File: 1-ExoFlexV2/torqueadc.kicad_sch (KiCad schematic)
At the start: 54 parts

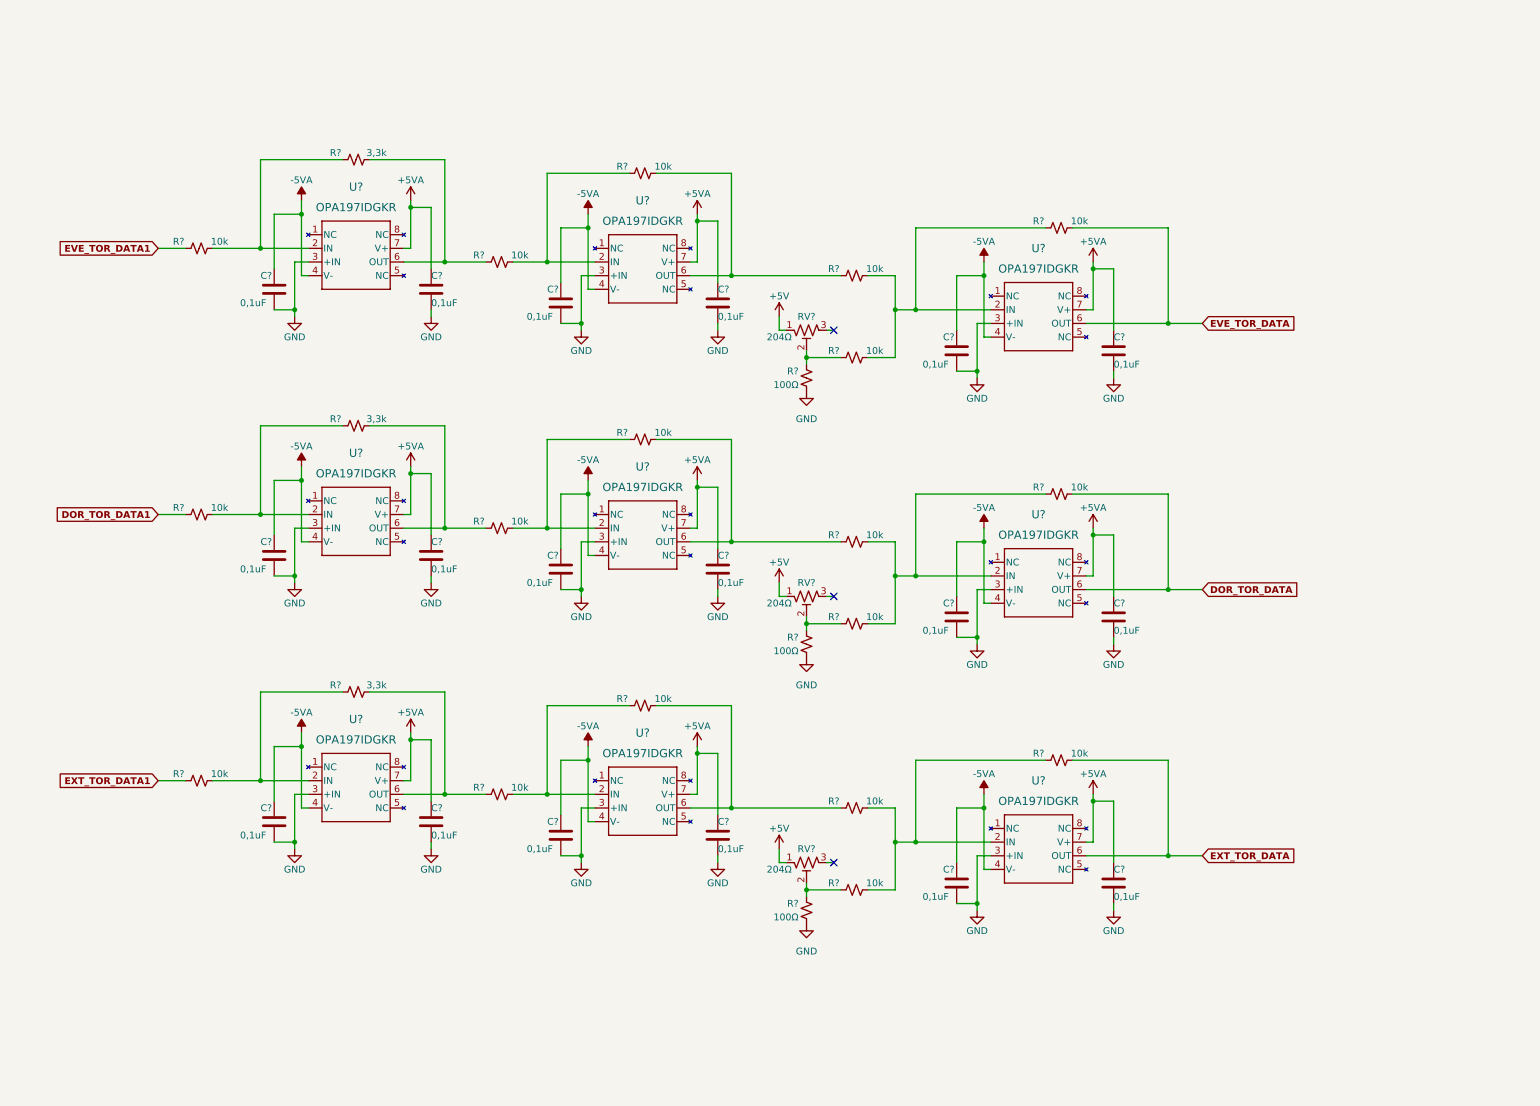
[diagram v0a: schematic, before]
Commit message: Chokes et RC
- Ajout des RF chokes
- Changement des résistance pour 0805
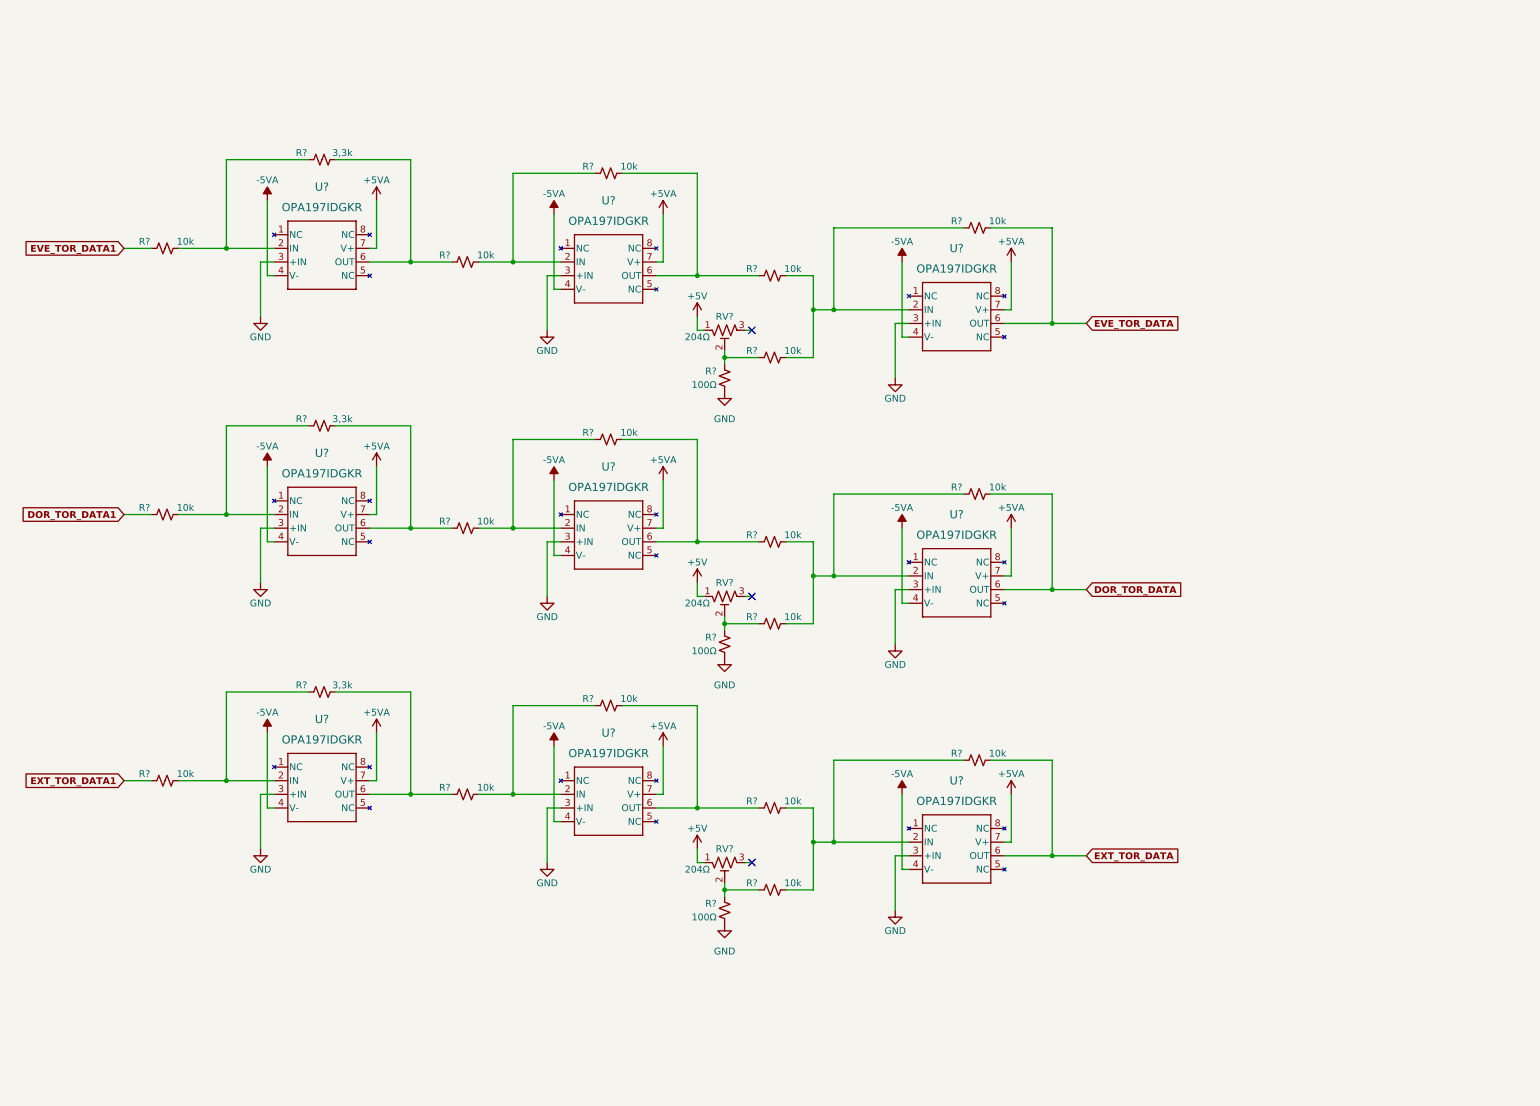
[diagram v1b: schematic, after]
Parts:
- removed C? (x18): 0,1uF, FootPrintLib:CAPC220145_88N_KEM, symbol Device:C
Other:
- moved on the sheet: R?, RV?, U?

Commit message: Trimmer et jumper
-Changement de symbole de jumper
-Ajout des des trimmer aux endroits nécessaires
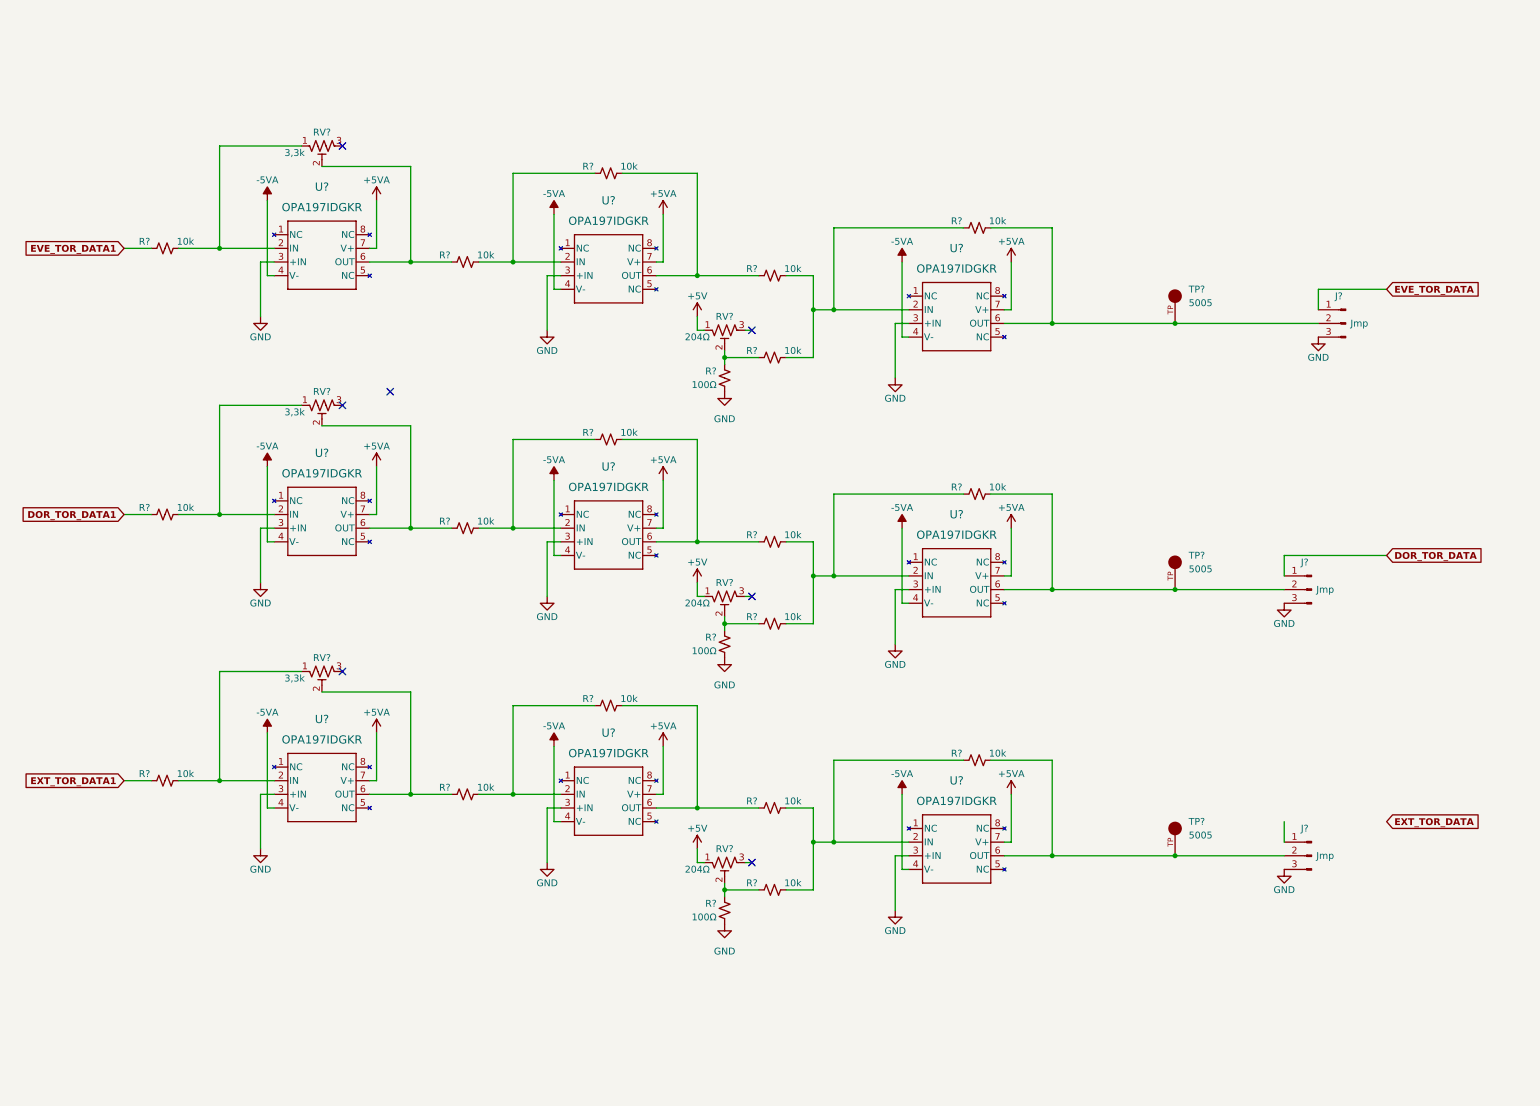
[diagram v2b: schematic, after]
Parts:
- removed R? (x3): 3,3k, Resistor_SMD:R_0805_2012Metric, symbol Device:R_Small_US
- added J? (x3): Jmp, symbol Connector:Conn_01x03_Male
- added RV? (x3): 3,3k, FootPrint:TRIM_3362P-1-102LF, symbol Device:R_Potentiometer_Trim_US
- added TP? (x3): 5005, FootPrint:KEYSTONE_5005, symbol SymLib:5005
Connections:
- net DOR_TOR_DATA: now also J?.1 (Pin_1); no longer R?.2, U?.6 (OUT)
- net EVE_TOR_DATA: now also J?.1 (Pin_1); no longer R?.2, U?.6 (OUT)
- net EXT_TOR_DATA: no longer R?.2, U?.6 (OUT)
- net GND: now also J?.3 (Pin_3), J?.3 (Pin_3), J?.3 (Pin_3)
- net at R?.2, U?.2 (IN): now also RV?.1 (x3)
- net at R?.1, U?.6 (OUT): now also RV?.2 (x3)
- new net: J?.2 (Pin_2), R?.2, TP?.TP, U?.6 (OUT) (x3)
- no-connect marks 3 -> 7

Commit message: Test points et notes
- Ajout de tous les tests point nécessaires
-  Ajoute des sections de notes dans chaque page
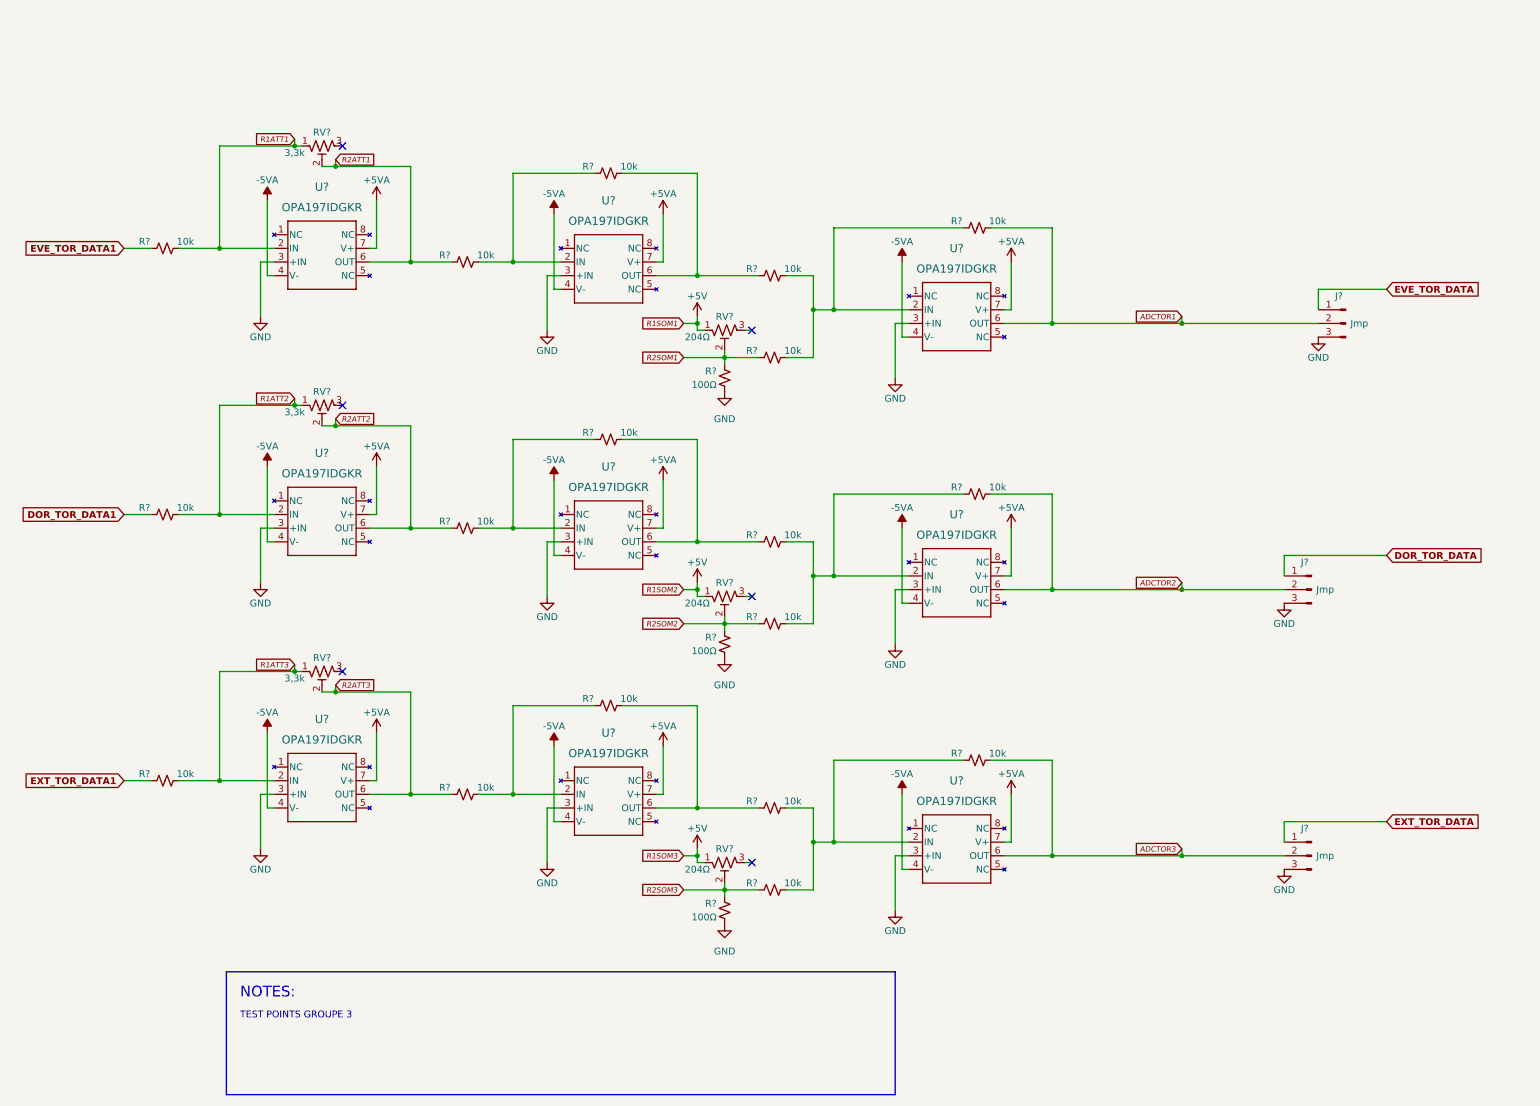
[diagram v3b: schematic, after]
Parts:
- removed TP? (x3): 5005, FootPrint:KEYSTONE_5005, symbol SymLib:5005
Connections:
- net EXT_TOR_DATA: now also J?.1 (Pin_1)
- net R2SOM2: now reaches R?.1, R?.2, RV?.2
- net ADCTOR3: now reaches J?.2 (Pin_2), R?.2, U?.6 (OUT)
- net R1ATT1: now reaches R?.2, RV?.1, U?.2 (IN)
- net R2SOM1: now reaches R?.1, R?.2, RV?.2
- net R1ATT3: now reaches R?.2, RV?.1, U?.2 (IN)
- net R2ATT3: now reaches R?.1, RV?.2, U?.6 (OUT)
- net R2ATT1: now reaches R?.1, RV?.2, U?.6 (OUT)
- net ADCTOR1: now reaches J?.2 (Pin_2), R?.2, U?.6 (OUT)
- net R2SOM3: now reaches R?.1, R?.2, RV?.2
- net R2ATT2: now reaches R?.1, RV?.2, U?.6 (OUT)
- net ADCTOR2: now reaches J?.2 (Pin_2), R?.2, U?.6 (OUT)
- net R1ATT2: now reaches R?.2, RV?.1, U?.2 (IN)
- no-connect marks 7 -> 6
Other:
- note added: "NOTES:"
- note added: "TEST POINTS GROUPE 3"

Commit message: Schématisation terminée
- Schéma terminé
- Passage vers le PCB
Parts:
- J86, J87, J88: renamed from J?; value Jmp -> Jumper; footprint (none) -> Connector_PinSocket_2.54mm:PinSocket_1x03_P2.54mm_Vertical; DESCRIPTION (none) -> CONN HEADER VERT 3POS 2.54MM; MANUFACTURER (none) -> Würth Elektronik; PACKAGE (none) -> Square 0.100" (2.54mm); PART NUMBER (none) -> 61300311121; TYPE (none) -> Through Hole
- R77, R78, R79, R80, R81, R82, R83, R84, R85, R87, R88, R91, R92, R93, R94, R95, R96, R97: renamed from R?; value 10k -> 1k 1% 1/10W; DESCRIPTION (none) -> 10 kOhms ±5% 0.125W, 1/8W Chip Resistor 0805 (2012 Metric) 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; MANUFACTURER (none) -> Panasonic Electronic Components; PACKAGE (none) -> 0805 (2012 Metric); PART NUMBER (none) -> ERJ-6GEYJ103V; TYPE (none) -> SMD
- R86, R89, R90: renamed from R?; value 100Ω -> 100Ω 1% 1/8W; DESCRIPTION (none) -> 100 Ohms ±1% 0.125W, 1/8W Chip Resistor 0805 (2012 Metric) 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; MANUFACTURER (none) -> Panasonic Electronic Components; PACKAGE (none) -> 0805 (2012 Metric); PART NUMBER (none) -> ERJ-6ENF1000V; TYPE (none) -> SMD
- RV21, RV22, RV23: renamed from RV?; value 3,3k -> Trim 1k; DESCRIPTION (none) -> Trimmer 1k 0,5W PC PIN TOP; MANUFACTURER (none) -> Bourns Inc.; PACKAGE (none) -> Rectangular - 0.275" x 0.260" Face; PART NUMBER (none) -> 3362P-1-102LF; TYPE (none) -> Through Hole
- RV24, RV25, RV26: renamed from RV?; value 204Ω -> Trim 1k; DESCRIPTION (none) -> Trimmer 1k 0,5W PC PIN TOP; MANUFACTURER (none) -> Bourns Inc.; PACKAGE (none) -> Rectangular - 0.275" x 0.260" Face; PART NUMBER (none) -> 3362P-1-102LF; TYPE (none) -> Through Hole
- U33, U34, U35, U36, U37, U38, U39, U40, U41: renamed from U?; value OPA197IDGKR -> OP-AMP; DESCRIPTION (none) -> General Purpose Amplifier 1 Circuit Rail-to-Rail 8-VSSOP; MANUFACTURER (none) -> Texas Instruments; PACKAGE (none) -> 8-TSSOP, 8-MSOP (0.118", 3.00mm Width); PART NUMBER (none) -> OPA197IDGKR; TYPE (none) -> SMD
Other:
- note added: "330Ω"
- note added: "9xOP-Amp : ±5VA @ 13,5mA 1,65VPot : 5V @ 53,57mA Total current : 5V @ 58mA +5VA @ 18mA -5VA @ 18mA"
- moved on the sheet: J86, J87, J88, R80, R83, R84, R85, R86, R87, R88, R95, R96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

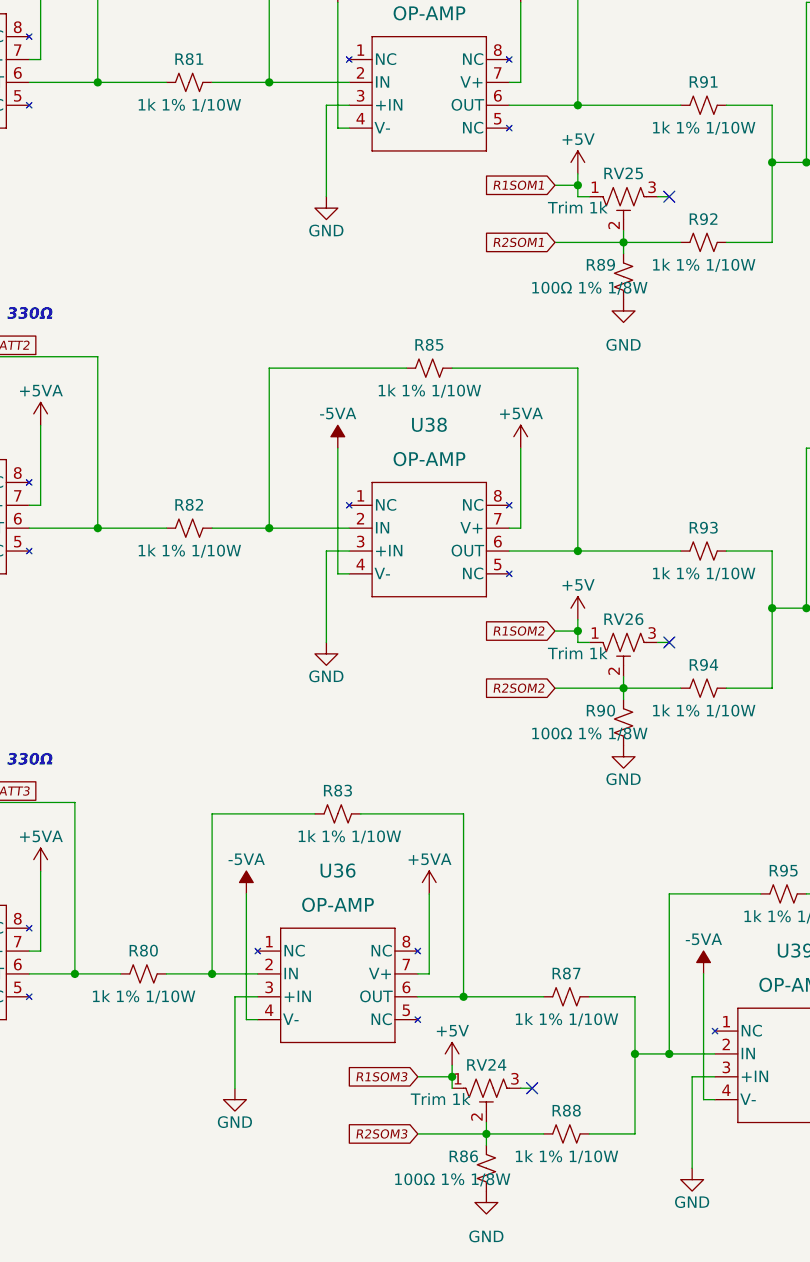
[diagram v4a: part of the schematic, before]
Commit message: Bug NetList
- Ajout de net-tie pour les GND et et les +5V
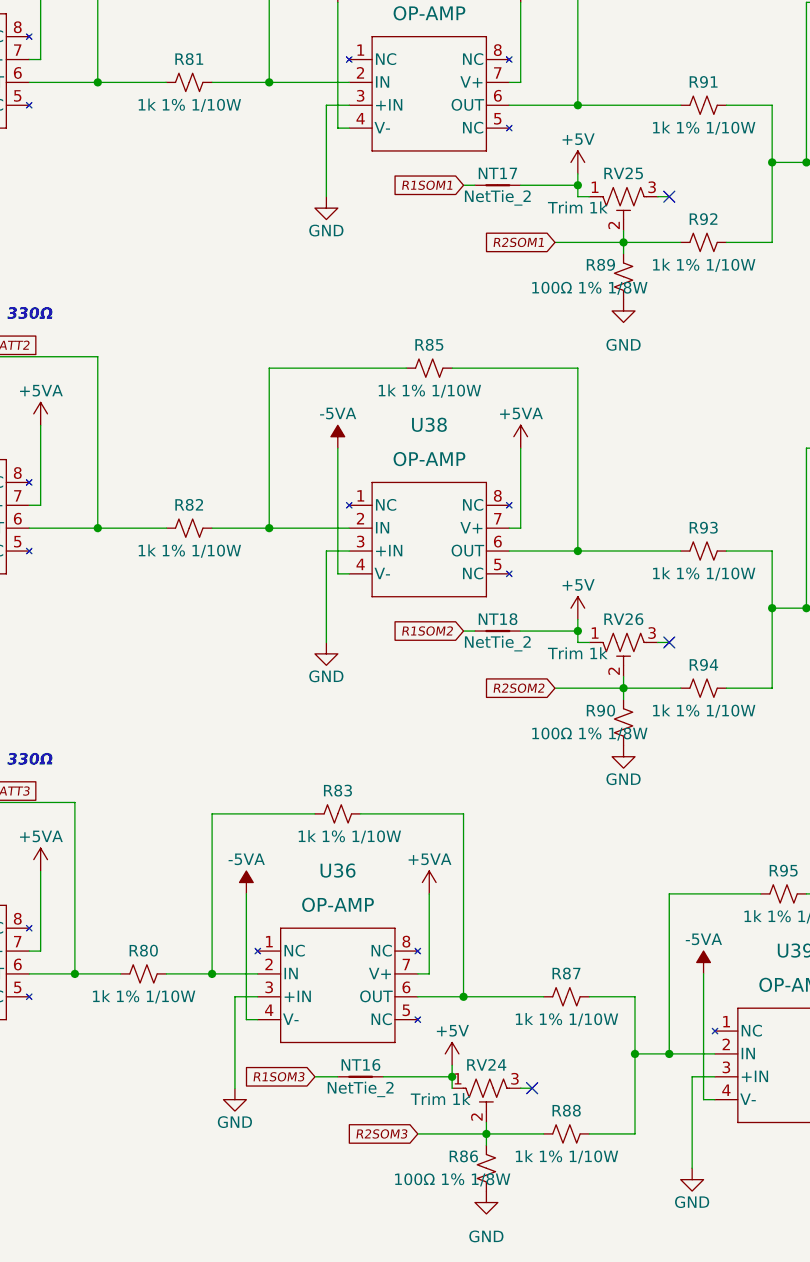
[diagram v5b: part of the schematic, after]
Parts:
- added NT16, NT17, NT18: NetTie_2, NetTie:NetTie-2_SMD_Pad0.5mm, symbol Device:NetTie_2
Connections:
- net +5V: now also NT16.2, NT17.2, NT18.2
- new net R1SOM1: NT17.1
- new net R1SOM2: NT18.1
- new net R1SOM3: NT16.1
